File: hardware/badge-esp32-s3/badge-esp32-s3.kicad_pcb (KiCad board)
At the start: 2 copper layers, 131.5 x 83.5 mm, 122 parts, among them CN1 B4B-PH-SM4-TB (LF)(SN), J1 Connector, USB-TYPE-C-16P, J2 Connector, USB-TYPE-C-16P, P1 PH-2A_C2319, P2 FPC 0.5MM 12P Pull type H2.0m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, Q1 SS8050 200-350, Q2 SS8050 200-350, Q3 HL2301A, SW1 TS-1088-AR02016, SW2 TS-1088-AR02016, SW3 SK-12F04-G050, SW4 TS665CJ, SW5 TS665CJ, SW6 TS665CJ, SW7 TS665CJ, SW8 TS665CJ, SW9 TS665CJ, U1 ESP32-S3-MINI-1-N8, U10 FH2.54-09-02PZD, U11 FH2.54-09-04PZD, U12 FH2.54-09-03PZD, U13 FH2.54-09-02PZD, U14 FH2.54-09-04PZD, U15 FH2.54-09-04PZD, U16 FH2.54-09-04PZD, U17 FH2.54-09-02PZD, U18 MMA8452QR1_C11360, U19 FH2.54-09-02PZD, U2 NCP167BMX330TBG, U3 CP2102N-A02-GQFN28R, U4 TP4056, U5 FH2.54-09-02PZD, U6 ZX-SH1.0-4PWT, U7 FH2.54-09-02PZD, U8 FH2.54-09-03PZD, U9 FH2.54-09-03PZD

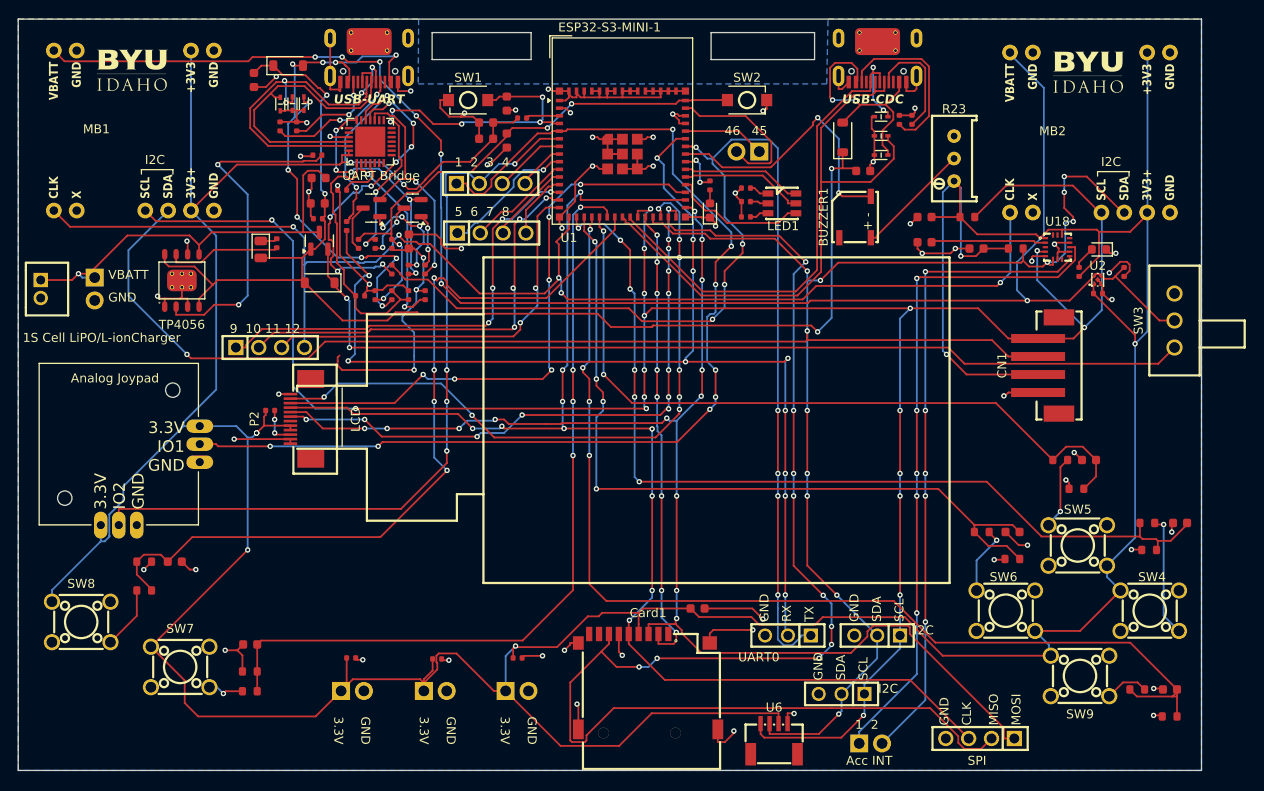
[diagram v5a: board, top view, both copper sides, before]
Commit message: Updated the audio schematic and traces.
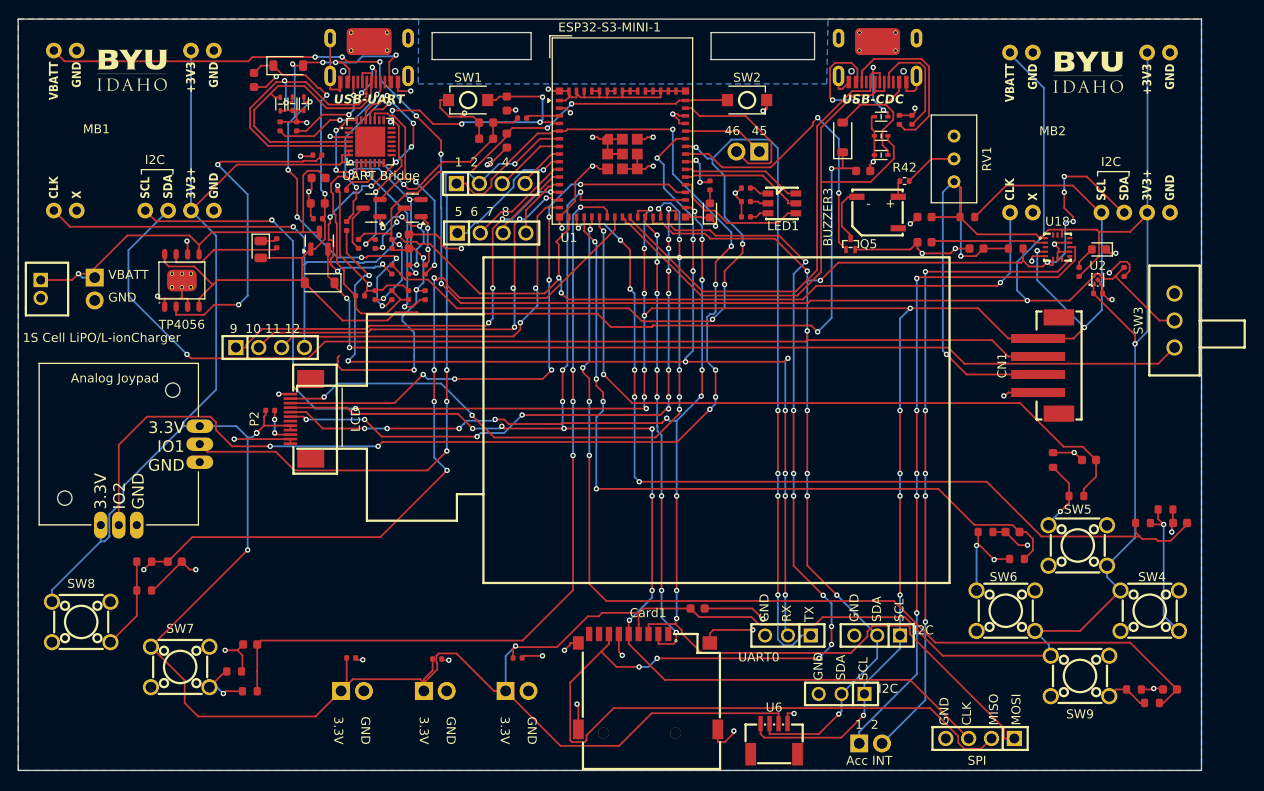
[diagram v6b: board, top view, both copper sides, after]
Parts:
- removed BUZZER1: MLT-5020, lcsc-lib:BUZ-SMD_L5.0-W5.5-P4.60
- removed R23: 3296W-1-103, lcsc-lib:RES-ADJ-TH_3P-L10.0-W10.0-P2.50-L
- added BUZZER3: MLT-5020, lcsc-lib:BUZ-SMD_L5.0-W5.5-P4.60, F.Cu at (179.0, 84.5)
- added Q5: DTC114E, misc-lib:SOT-523_L1.6-W0.8-P1.00-BR, F.Cu at (176.0, 88.0)
- added R42: 27Ω, Resistor_SMD:R_0402_1005Metric, F.Cu at (182.0, 81.0)
- added RV1: 1000Ω, Potentiometer_THT:Potentiometer_Bourns_3296W_Vertical, F.Cu at (187.5, 81.1)
- moved R28 3.08 mm to (208.5, 119.0)
- moved R33 2.80 mm to (107.5, 135.5)
- moved R27 2.52 mm to (211.0, 117.5), turned to 0 degrees
- moved R38 2.47 mm to (209.5, 139.0), turned to 0 degrees
- moved R34 2.20 mm to (109.2, 137.7), turned to 0 degrees
- moved R29 0.80 mm to (198.5, 112.0), turned to 90 degrees
- moved R30 0.80 mm to (201.1, 116.0), turned to 0 degrees
- moved R32 0.52 mm to (194.5, 123.0), turned to 0 degrees
- moved R31 0.42 mm to (191.0, 120.0), turned to 0 degrees
- moved R37 0.36 mm to (207.5, 137.5), turned to 0 degrees
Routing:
- net /GPIO1: track 123.3 -> 143.4 mm
- net GND: track 241.9 -> 260.6 mm
- net Net-(BUZZER1-+): track 13.0 -> 0.00 mm
- net /GPIO2: track 87.7 -> 76.5 mm
- net /GPIO15: track 121.9 -> 114.6 mm, vias 5 -> 4
- net Net-(BUZZER3--): track 0.00 -> 6.30 mm
- net /GPIO18: track 92.4 -> 86.3 mm
- net Net-(R42-Pad1): track 0.00 -> 6.01 mm
- net /GPIO14: track 88.7 -> 84.8 mm, vias 5 -> 4
- net Net-(SW6-D): track 7.78 -> 10.9 mm, vias 1 -> 2
- net /GPIO42: track 30.8 -> 33.7 mm
- net Net-(SW8-D): track 6.96 -> 9.84 mm
- net Net-(SW7-D): track 4.07 -> 6.72 mm
- net Net-(SW4-D): track 13.6 -> 16.0 mm
- net /GPIO13: track 102.9 -> 100.9 mm, vias 7 -> 6
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
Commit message: Fixed nested git repo issue in backups
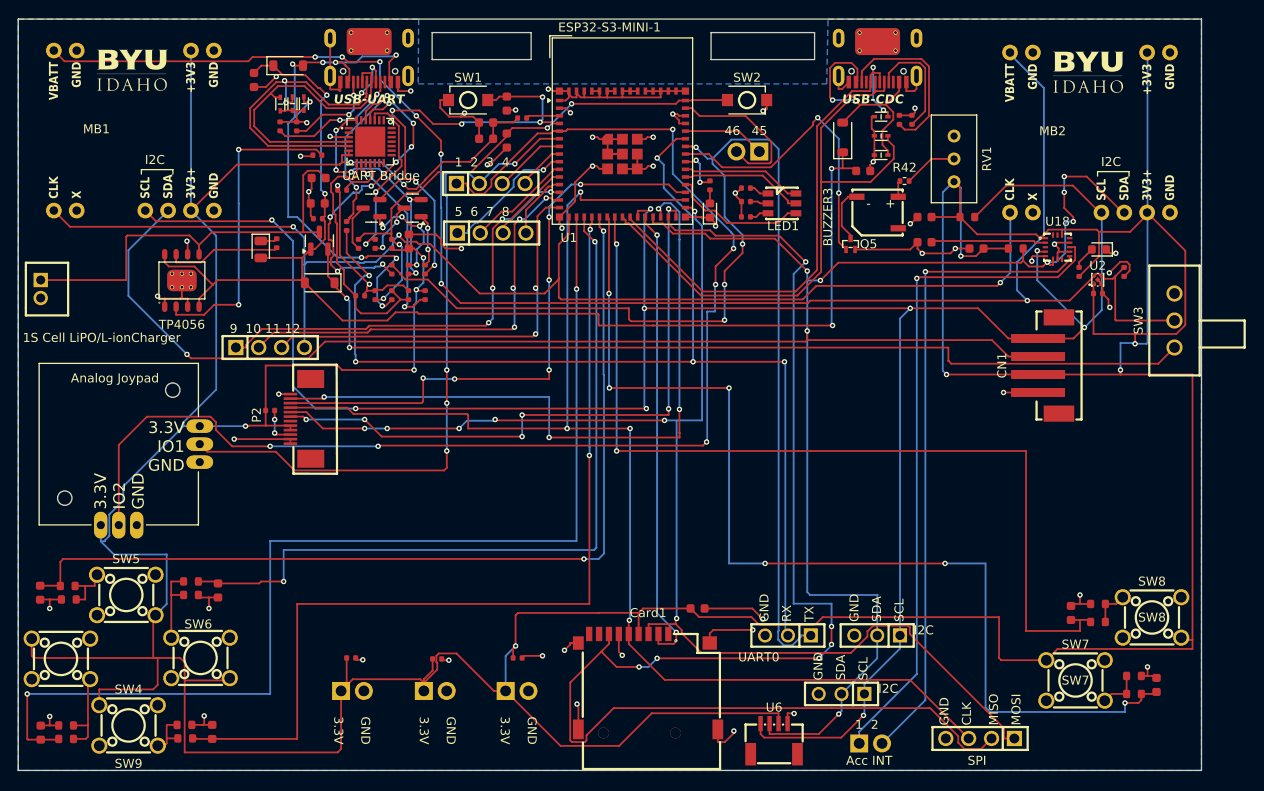
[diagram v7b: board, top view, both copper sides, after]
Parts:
- removed LCD: OLED-SMD_HS20HS072RX, lcsc-lib:OLED-SMD_HS20HS072RX
- removed U5: FH2.54-09-02PZD, lcsc-lib:HDR-TH_2P-P2.54-V-M-5
- moved C18 128.7 mm to (86.0, 142.3), turned to 90 degrees
- moved R27 124.5 mm to (88.8, 141.5), turned to 180 degrees
- moved R28 122.1 mm to (88.8, 143.0)
- moved SW4 121.1 mm to (88.2, 134.1)
- moved SW8 119.0 mm to (209.5, 129.5), turned to 180 degrees
- moved C19 117.5 mm to (85.9, 126.8), turned to -90 degrees
- moved R30 112.5 mm to (89.0, 126.0), turned to 180 degrees
- moved R29 110.5 mm to (89.1, 127.5), turned to 180 degrees
- moved R38 107.5 mm to (102.1, 142.9)
- moved C23 106.5 mm to (105.1, 142.2), turned to 90 degrees
- moved R36 106.2 mm to (203.5, 130.0), turned to 180 degrees
- moved R35 106.0 mm to (203.5, 128.0), turned to 180 degrees
- moved SW5 105.9 mm to (95.5, 127.0)
- moved SW9 105.9 mm to (95.8, 141.5)
- moved R37 105.6 mm to (102.0, 141.4)
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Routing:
- net +3.3V: track 525.4 -> 619.6 mm, vias 12 -> 11
- net /GPIO17: track 89.5 -> 117.4 mm, vias 4 -> 6
- net /GPIO16: track 80.9 -> 102.9 mm
- net /GPIO13: track 100.9 -> 122.3 mm, vias 6 -> 2
- net /GPIO18: track 86.3 -> 101.1 mm, vias 5 -> 2
- net /GPIO15: track 114.6 -> 103.0 mm, vias 4 -> 2
- net Net-(SW4-D): track 16.0 -> 10.1 mm, vias 1 -> 0
- net Net-(SW8-D): track 9.84 -> 4.24 mm
- net /GPIO47: track 253.2 -> 257.6 mm, vias 13 -> 9
- net GND: track 260.6 -> 256.3 mm
- net /GPIO36: track 148.2 -> 145.1 mm, vias 10 -> 4
- net /GPIO33: track 74.0 -> 76.9 mm, vias 8 -> 4
- net +4V: track 182.8 -> 185.6 mm
- net Net-(U4-PROG): track 37.7 -> 35.1 mm
- net /GPIO34.: track 155.2 -> 157.6 mm, vias 10 -> 6
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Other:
- board text added: "SW7"
- board text added: "SW8"
- board text removed: "VBATT"
